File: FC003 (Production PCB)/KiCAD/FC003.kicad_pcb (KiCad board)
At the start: 2 copper layers, 150 x 32 mm, 62 parts, among them IC1 MSP430G2202, IC10 SC52-11, IC11 SC52-11, IC12 SC52-11, IC2 4017, IC3 74HC4060, IC4 ULN2803A, IC5 SC52-11, IC6 SC52-11, IC7 SC52-11, IC8 SC52-11, IC9 SC52-11, J1 JTAG, J2 IN, J3 PWR, J4 ACCESSORY, J5 EXT CLK, J6 HF SRC, SW1 DIPSW-8, X1 4.194304MHz

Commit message: FC003 (Production PCB) - intermittent changes
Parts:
- moved J3 8.82 mm to (240.0, 128.9), turned to 180 degrees
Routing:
- net N-0000021: track 207.8 -> 154.9 mm, vias 7 -> 3
- net N-0000024: track 181.2 -> 156.6 mm, vias 6 -> 1
- net N-0000023: track 170.2 -> 152.2 mm, vias 6 -> 0
- net GND: track 214.3 -> 227.2 mm
- net VCC: track 148.5 -> 161.0 mm
- net N-0000022: track 207.1 -> 196.1 mm
- net N-0000073: track 174.1 -> 172.0 mm
- net N-0000060: track 22.4 -> 20.3 mm
- net N-0000027: track 31.8 -> 30.4 mm
- net N-0000019: track 124.9 -> 123.7 mm, vias 7 -> 2
- net N-000006: track 95.7 -> 94.8 mm
- net N-0000032: track 29.7 -> 28.9 mm
- net N-0000026: track 22.4 -> 21.6 mm
- net N-0000018: track 115.9 -> 115.1 mm
- net N-0000028: track 19.9 -> 19.3 mm
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
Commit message: Hardware Design finished Casing (SOB) added design/caes panelize added
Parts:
- added C8: 100uF/16V, C1P_D2.7, F.Cu at (247.0, 110.5)
- added C9: 22uF/16V, C1P_D2.7, F.Cu at (240.7, 123.2)
- added G***: LOGO, OSHWLOGO0.3IN, F.Cu at (106.6, 100.8)
- added J15: PSU, PWR_3.5, F.Cu at (240.7, 106.7)
- added J16: EN_PR, HDR-2, F.Cu at (108.6, 119.4)
- added J17: IN_DIG, HDR-2, F.Cu at (103.5, 109.6)
- added U13: TS2950CT, TO-92_V, F.Cu at (247.0, 118.1)
- J1: value JTAG -> SBW
- moved J4 1.91 mm to (234.3, 109.2)
- moved J5 0.38 mm to (103.5, 121.0)
- moved J6 0.38 mm to (103.5, 114.7)
- renumbered IC1 to U1, IC10 to U10, IC11 to U11, IC12 to U12, IC2 to U2, IC3 to U3, IC4 to U4, IC5 to U5, IC6 to U6, IC7 to U7, IC8 to U8, IC9 to U9
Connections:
- D10 pad 2: N-0000048 -> N-0000040
- D9 pad 1: N-0000048 -> N-0000040
- J1 pad 4: (no net) -> VCC
- J4 pad 12: (no net) -> VDD
- R5 pad 2: N-0000048 -> N-0000040
- U1 pad 2: N-0000048 -> N-0000038
- U1 pad 6: N-0000048 -> N-0000038
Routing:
- net N-0000038: track 0.00 -> 43.9 mm
- net N-0000074: track 154.9 -> 198.7 mm, vias 3 -> 7
- net VCC: track 161.0 -> 191.8 mm
- net N-0000048: track 30.8 -> 0.00 mm
- net VDD: track 0.00 -> 16.3 mm
- net GND: track 227.2 -> 239.2 mm
- net N-0000040: track 0.00 -> 11.3 mm
- net N-0000077: track 216.5 -> 211.5 mm
- net N-0000049: track 172.0 -> 175.3 mm
- net N-0000073: track 123.7 -> 121.6 mm
- net N-0000071: track 196.1 -> 194.2 mm
- net N-0000076: track 115.1 -> 113.2 mm
- net N-0000072: track 156.6 -> 154.7 mm
- net N-0000044: track 152.2 -> 150.3 mm
- net N-0000039: track 79.1 -> 77.2 mm
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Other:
- board text added: "FC003 - DESIGNED BY SUF"

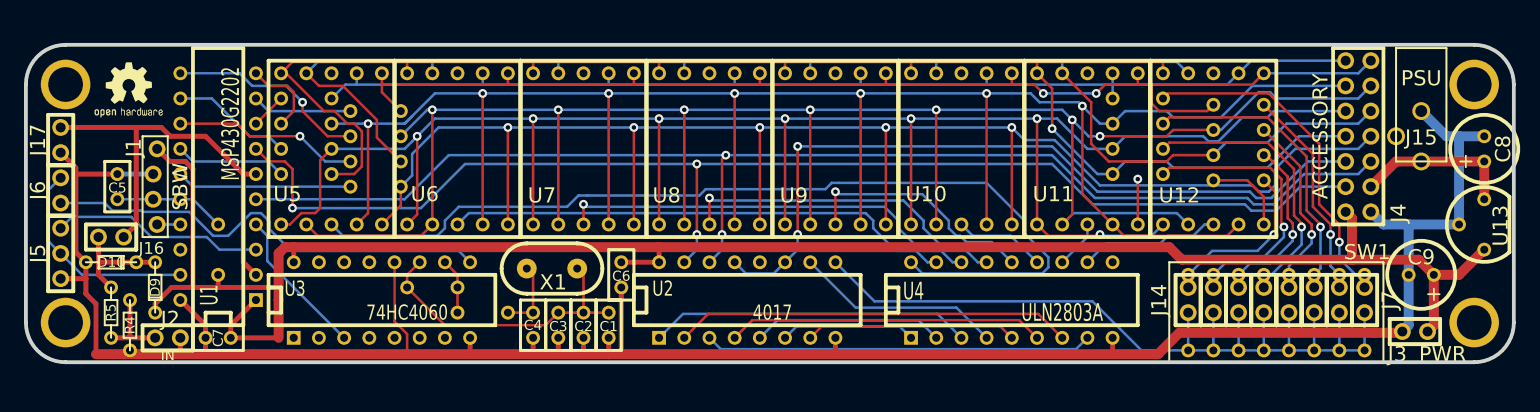
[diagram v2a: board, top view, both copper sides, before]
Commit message: Hardware: Minor PCB modifications SOB manufacturing plans
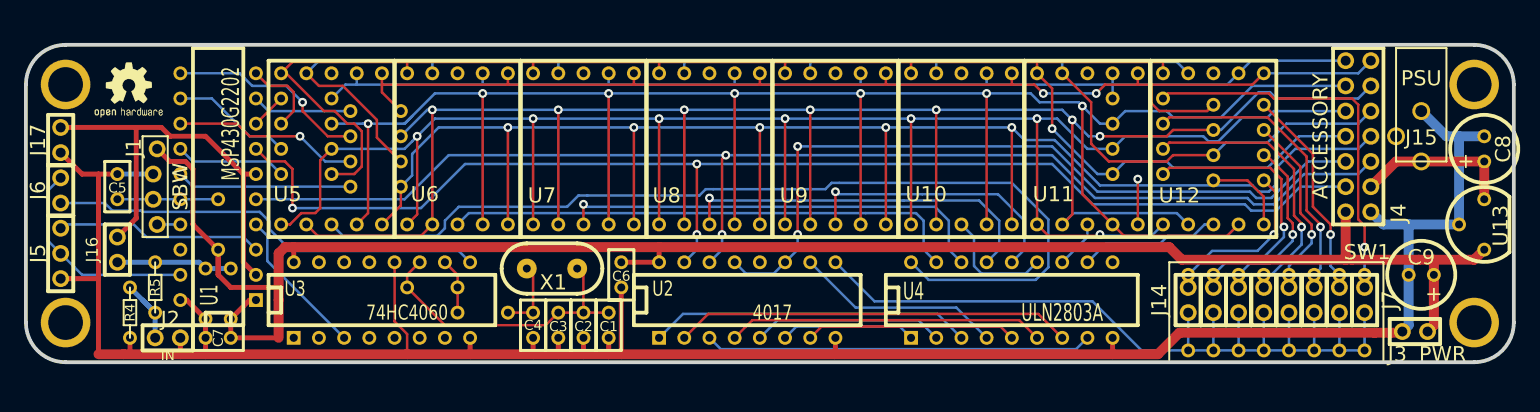
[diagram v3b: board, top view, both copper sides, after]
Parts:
- D10, D9: moved to B.Cu
- moved D10 10.0 mm to (118.1, 125.1), turned to 90 degrees
- moved D9 7.65 mm to (120.7, 125.1)
- moved R5 5.12 mm to (113.0, 124.5)
- moved R3 2.54 mm to (119.4, 118.1)
- moved J16 1.42 mm to (109.2, 120.7), turned to 90 degrees
- moved R4 1.27 mm to (110.5, 127.0)
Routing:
- net VCC: track 191.8 -> 185.8 mm
- net N-0000035: track 35.0 -> 39.0 mm
- net N-000001: track 33.7 -> 37.5 mm
- net N-000005: track 24.5 -> 28.3 mm
- net GND: track 239.2 -> 241.9 mm
- net N-000006: track 9.20 -> 11.9 mm
- net N-000002: track 94.8 -> 96.8 mm
- net N-0000021: track 46.1 -> 44.2 mm
- net N-000003: track 51.2 -> 52.5 mm
- net N-000004: track 43.0 -> 44.3 mm
- net N-0000062: track 11.2 -> 10.2 mm
- net N-0000016: track 21.5 -> 20.9 mm
